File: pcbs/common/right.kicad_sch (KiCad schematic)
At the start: 88 parts

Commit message: Update for rev4.1.0
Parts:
- removed rF?: BSMD0603-050-12V, Fuse:Fuse_0603_1608Metric, symbol Device:Fuse
- removed rJ?: ST-0277D00-052-142, kbd_local:ST-0277D00-052-142, symbol Connector_Audio:AudioJack4
- removed rZD?: ESD5Z5V0C, Diode_SMD:D_SOD-523, symbol Diode:ESD5Zxx
- added J2: TRS, kbd_local:PJ-398A-5A_PJ-399B-6A, symbol Connector_Audio:AudioJack3
- added R?: 5.6k, Resistor_SMD:R_0402_1005Metric, symbol Device:R_Small
- added R?: 10K, Resistor_SMD:R_0402_1005Metric, symbol Device:R_Small
- added ZD?: RB521S30T1G, Diode_SMD:D_SOD-523, symbol Diode:ESD5Zxx
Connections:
- net +5VR: now also J2.T, ZD?.1 (K)
- net GNDR: now also J2.S, R?.2
- net TX: now also J2.R
- net VBUSR: now also R?.1, ZD?.2 (A)
- net RX renamed USB_VBUS_PIN
- net USB_VBUS_PIN: now also R?.1, R?.2
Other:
- note added: "TRS"
- note removed: "T(4,5), R1(3), R2(2), S(1)"
- note removed: "TRRS"
- note removed: "left R1:RX, R2:TX right R1:TX, R2:RX"

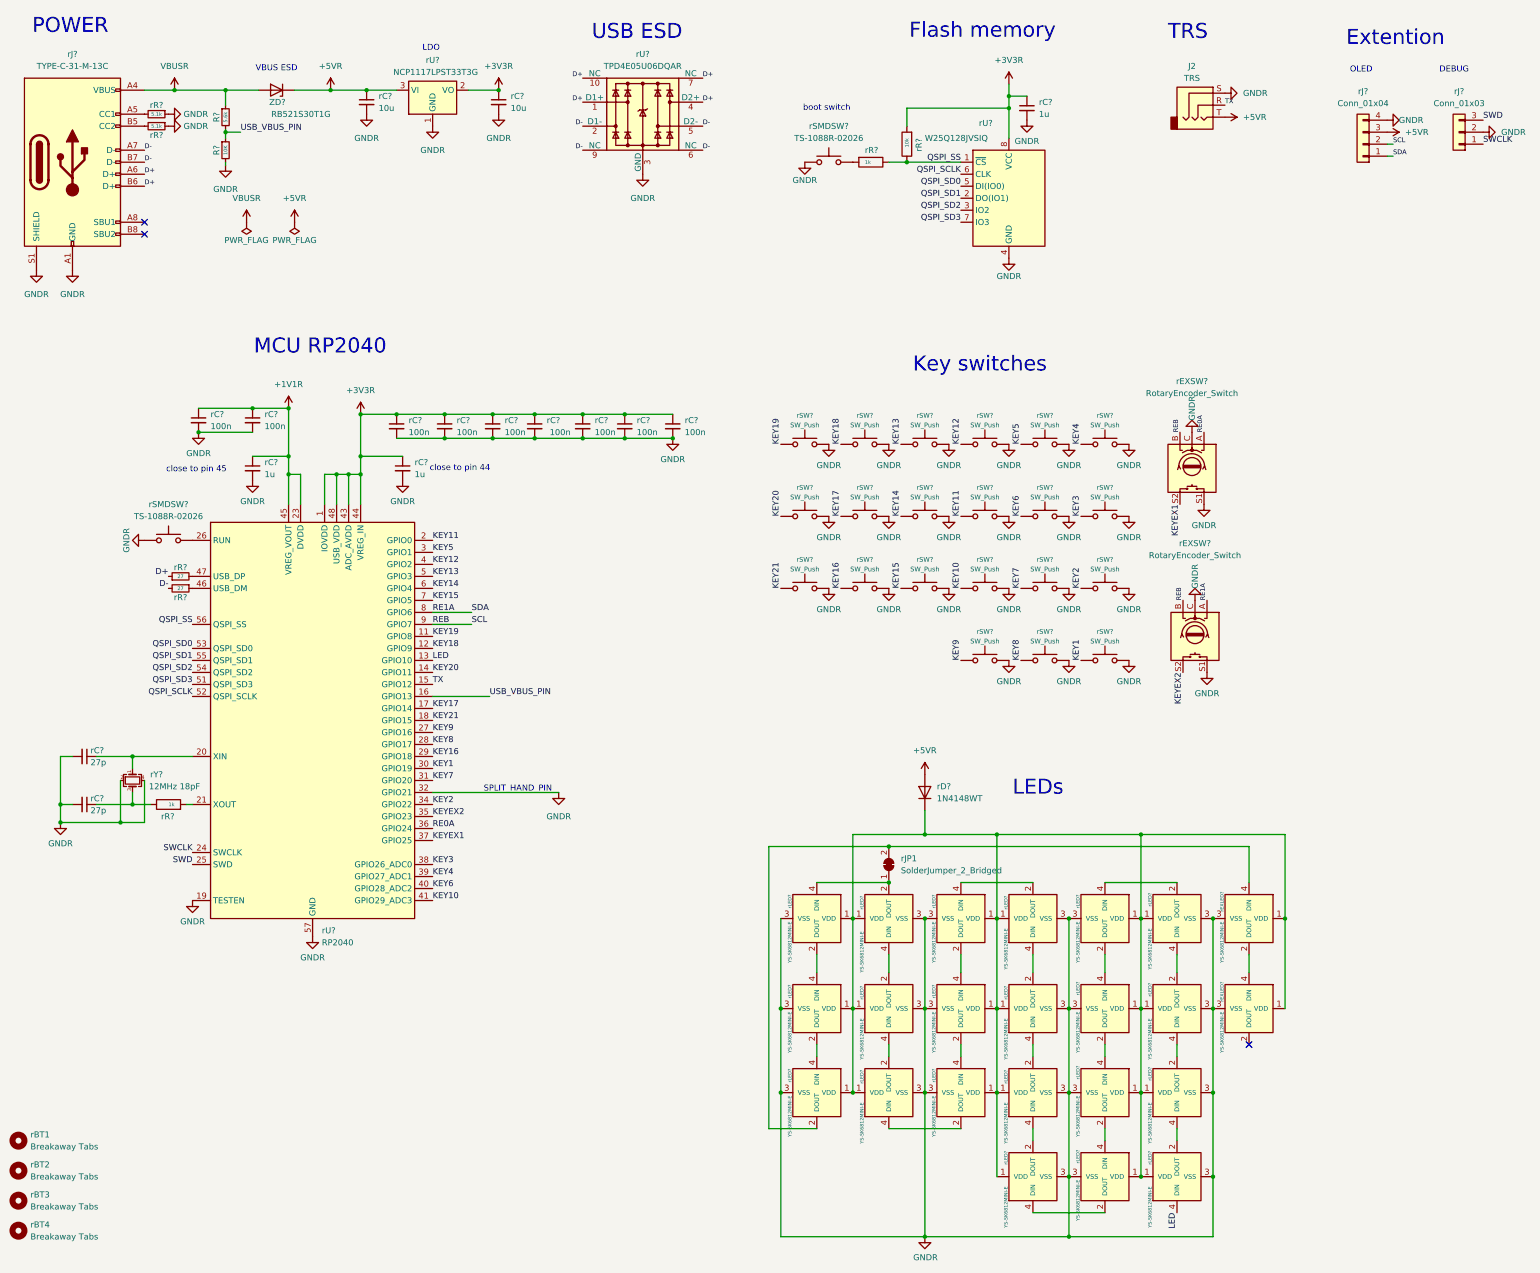
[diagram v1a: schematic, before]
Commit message: Change 4 layer left side
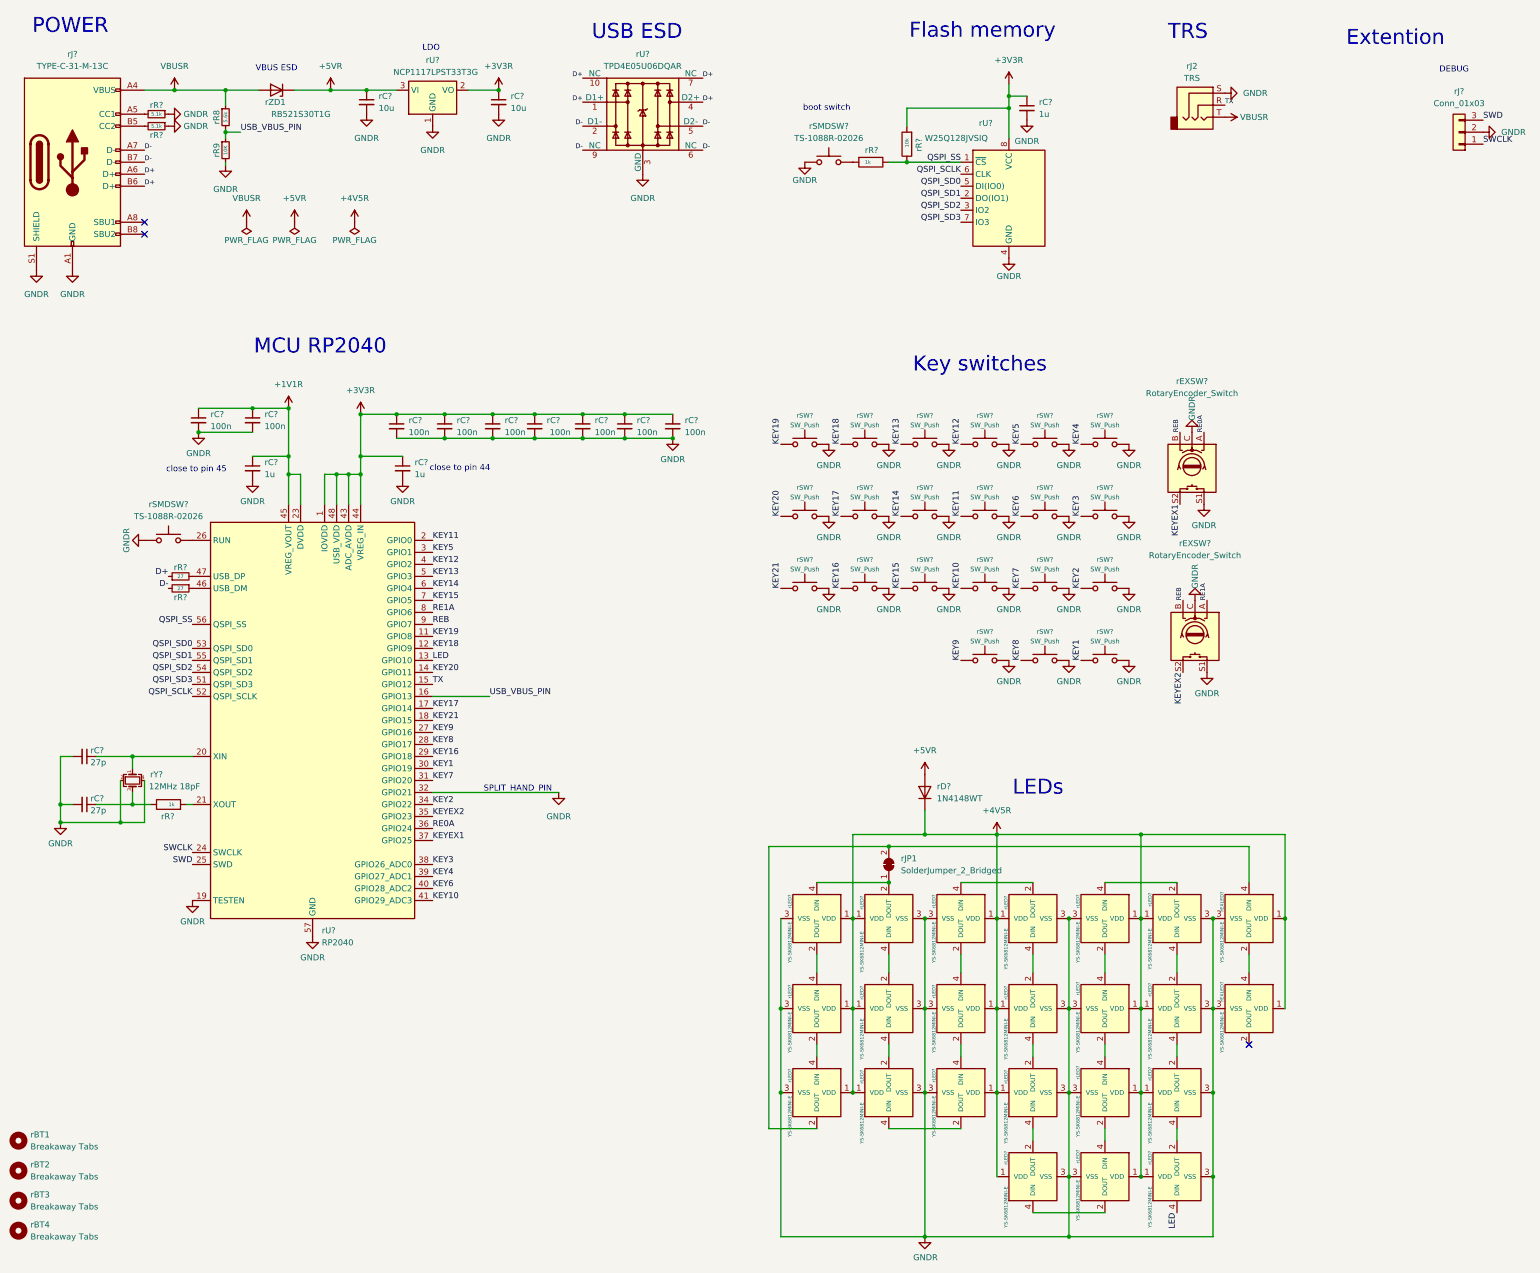
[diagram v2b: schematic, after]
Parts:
- removed rJ?: Conn_01x04, kbd_local:OLED, symbol Connector_Generic:Conn_01x04
- gave numbers to parts that had none: 3
- renumbered J2 to rJ2
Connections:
- net +5VR: no longer rJ2.T
- net VBUSR: now also rJ2.T
- net +4V5: now reaches rD?.1 (K), rEXLED?.1 (VDD), rEXLED?.1 (VDD), rLED?.1 (VDD), rLED?.1 (VDD), rLED?.1 (VDD), rLED?.1 (VDD), rLED?.1 (VDD), rLED?.1 (VDD), rLED?.1 (VDD), rLED?.1 (VDD), rLED?.1 (VDD), rLED?.1 (VDD), rLED?.1 (VDD), rLED?.1 (VDD), rLED?.1 (VDD), rLED?.1 (VDD), rLED?.1 (VDD), rLED?.1 (VDD), rLED?.1 (VDD), rLED?.1 (VDD), rLED?.1 (VDD), rLED?.1 (VDD), rLED?.1 (VDD)
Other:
- note removed: "OLED"
